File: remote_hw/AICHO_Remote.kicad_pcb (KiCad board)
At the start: 2 copper layers, 14 parts, among them J3 RJ45, U1 TPS54302

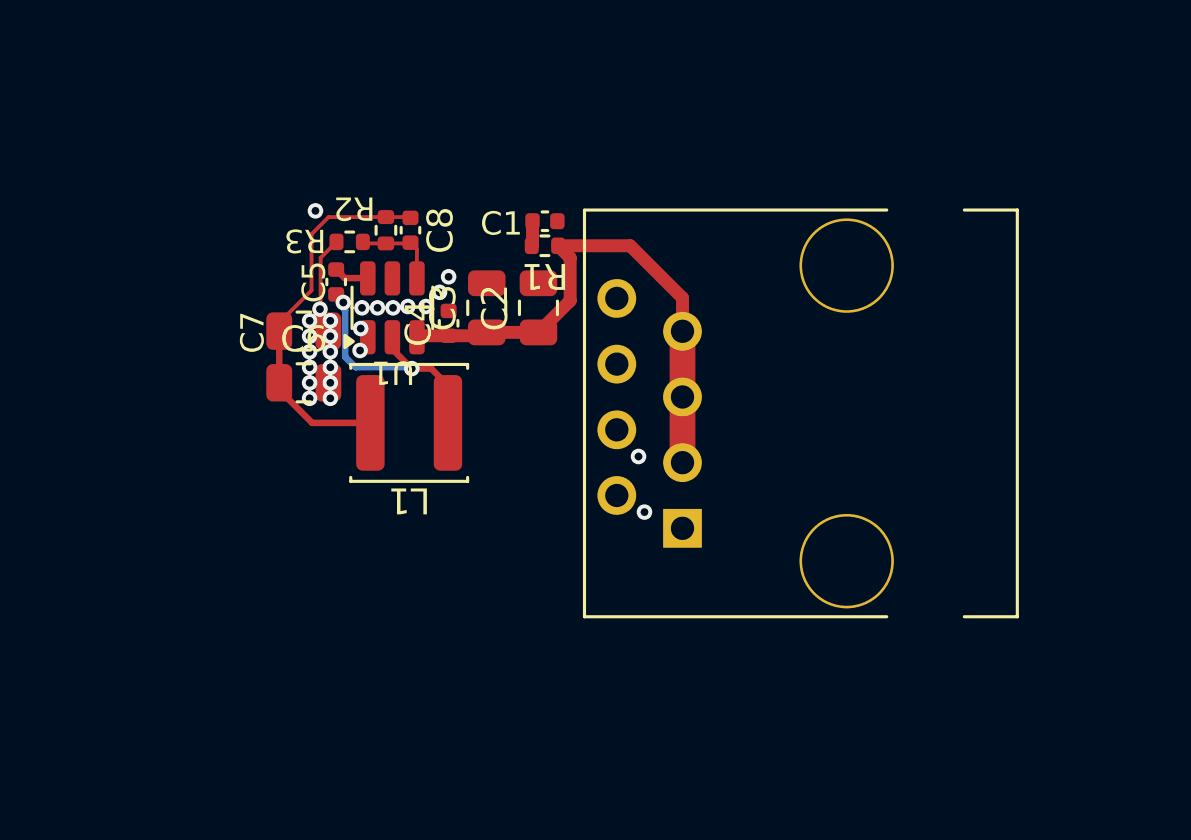
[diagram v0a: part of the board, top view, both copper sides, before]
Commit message: remote_hw: Finish layout & routing
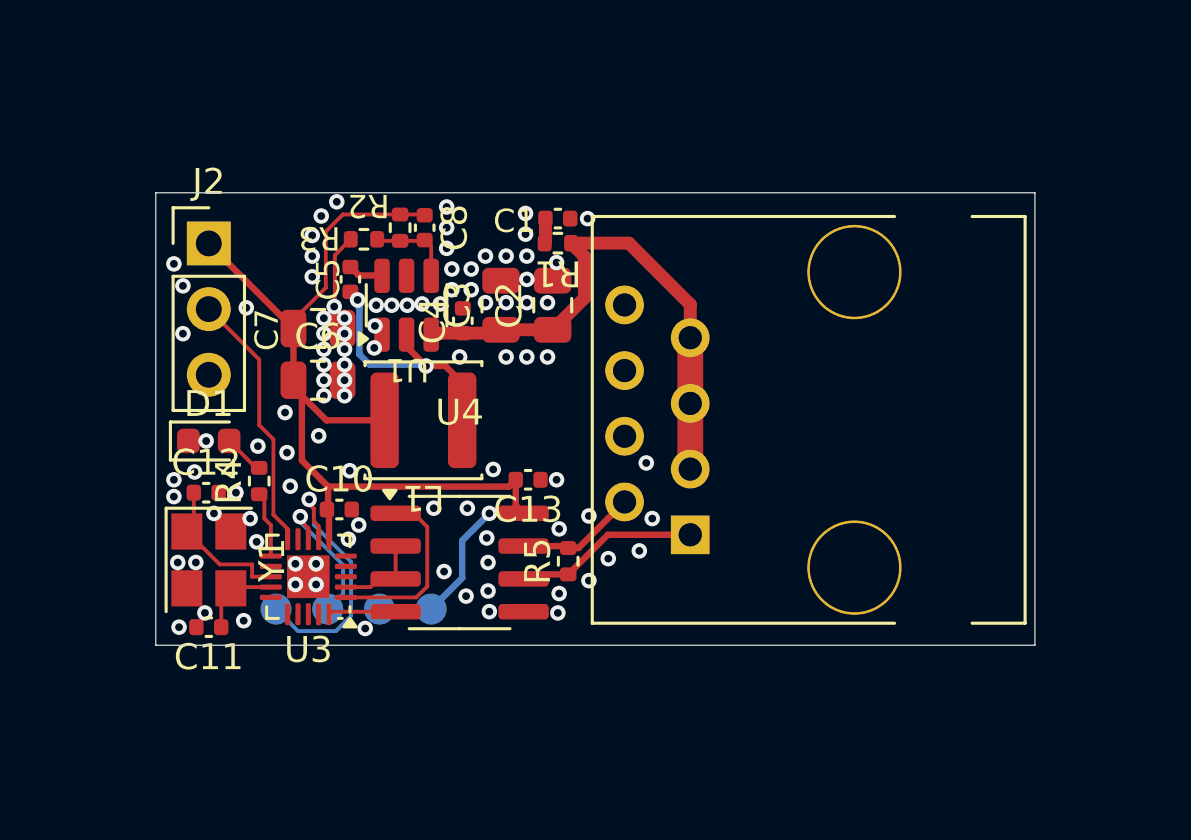
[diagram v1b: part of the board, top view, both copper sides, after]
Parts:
- added C10: 100n, Capacitor_SMD:C_0402_1005Metric, F.Cu at (69.1, 51.5)
- added C11: 15p, Capacitor_SMD:C_0402_1005Metric, F.Cu at (64.0, 56.0)
- added C12: 15p, Capacitor_SMD:C_0402_1005Metric, F.Cu at (64.0, 50.9)
- added C13: 100n, Capacitor_SMD:C_0402_1005Metric, F.Cu at (76.4, 50.4)
- added D1: White, LED_SMD:LED_0603_1608Metric, F.Cu at (64.0, 48.9)
- added J1: Conn_01x04, TestPoints_P2.00:TestPoints_1x04_P2.00, B.Cu at (69.7, 55.4)
- added J2: Conn_01x03_Pin, Connector_PinHeader_2.54mm:PinHeader_1x03_P2.54mm_Vertical, F.Cu at (64.0, 41.2)
- added R4: 6.8k, Resistor_SMD:R_0402_1005Metric, F.Cu at (66.0, 50.4)
- added R5: 100, Resistor_SMD:R_0402_1005Metric, F.Cu at (78.0, 53.5)
- added U3: PY32F003F18U6, Package_DFN_QFN:QFN-20-1EP_3x3mm_P0.4mm_EP1.65x1.65mm, F.Cu at (67.9, 54.1)
- added U4: SP485E, Package_SO:SOIC-8_3.9x4.9mm_P1.27mm, F.Cu at (73.8, 53.5)
- added Y1: 16MHz 9pF, Crystal:Crystal_SMD_3225-4Pin_3.2x2.5mm, F.Cu at (64.0, 53.5)
- moved C5 0.56 mm to (69.5, 42.6)
- moved C6 0.56 mm to (68.3, 46.5)
- moved C7 0.56 mm to (68.3, 44.5)
- moved C8 0.56 mm to (72.4, 40.6)
- moved C2 0.56 mm to (77.3, 43.6)
- moved C3 0.56 mm to (75.3, 43.6)
- moved L1 0.56 mm to (72.3, 48.0)
- moved R2 0.56 mm to (71.5, 40.6)
- moved R3 0.56 mm to (70.0, 41.0)
- moved U1 0.56 mm to (71.7, 43.6)
- moved C4 0.56 mm to (73.9, 44.2)
- moved C1 0.51 mm to (77.5, 40.2)
- moved R1 0.51 mm to (77.5, 41.2)
- moved J3 0.39 mm to (82.7, 52.5)
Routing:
- net +5V: track 14.7 -> 40.9 mm, vias 0 -> 1
- net /SWDIO: track 0.00 -> 10.4 mm, vias 0 -> 1
- net /LIGHT_SIG: track 0.00 -> 10.2 mm
- net /RS485_A: track 0.00 -> 7.15 mm
- net /UART_RX: track 0.00 -> 7.07 mm
- net Net-(U3-PF0): track 0.00 -> 5.87 mm
- net /SWCLK: track 0.00 -> 5.51 mm, vias 0 -> 1
- net /RS485_B: track 0.00 -> 4.67 mm
- net /DE: track 0.00 -> 3.33 mm
- net Net-(U3-PF1): track 0.00 -> 3.31 mm
- net /UART_TX: track 0.00 -> 2.61 mm
- net /ACT_LED: track 0.00 -> 2.58 mm
- net Net-(D1-A): track 0.00 -> 1.59 mm
- net GND: vias 25 -> 97
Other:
- board outline added: 34 x 17.5 mm

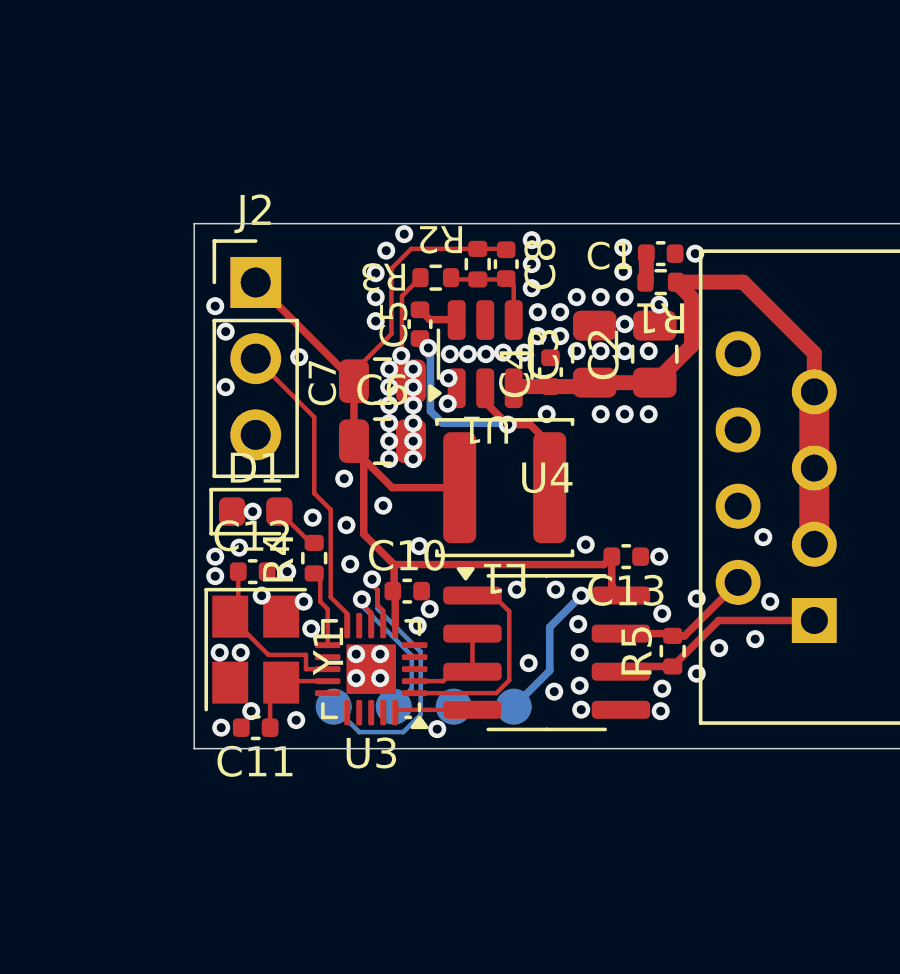
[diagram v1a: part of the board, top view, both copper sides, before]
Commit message: remote_hw: Adjust silkscreen
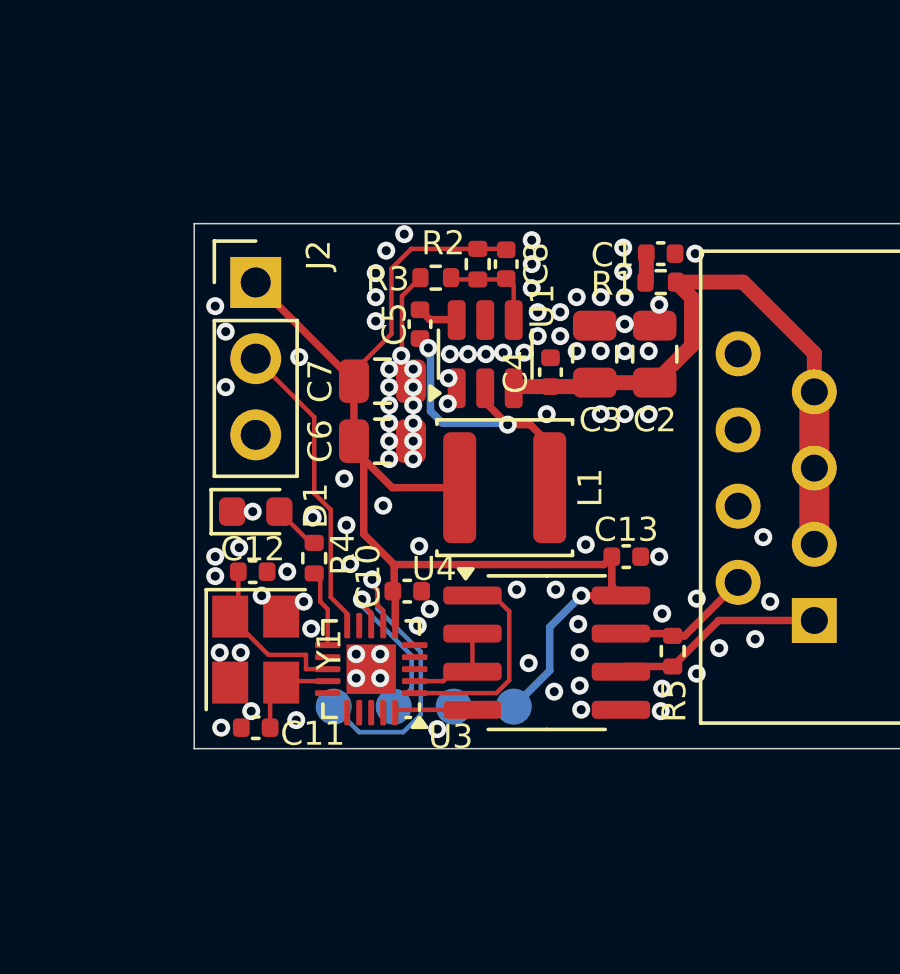
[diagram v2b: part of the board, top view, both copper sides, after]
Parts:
- added G***: LOGO, LOGO, B.Cu at (93.3, 44.4)
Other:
- board text added: "<25-"
- board text added: ">"
- board text added: "Rev. 1"
- board text added: "白露"

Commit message: remote_hw: Revise details
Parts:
- moved G*** 0.25 mm to (93.3, 44.6)
- renumbered U3 to U2, U4 to U3
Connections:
- U2 pad 12: unconnected-(U3-PF4-Pad12) -> (no net)
- U2 pad 15: unconnected-(U3-PF2-Pad15) -> (no net)
- U2 pad 16: unconnected-(U3-PA0-Pad16) -> (no net)
- U2 pad 17: unconnected-(U3-PA1-Pad17) -> (no net)
- U2 pad 18: unconnected-(U3-PA2-Pad18) -> (no net)
- U2 pad 19: unconnected-(U3-PA3-Pad19) -> (no net)
- U2 pad 3: unconnected-(U3-PA7-Pad3) -> (no net)
- U2 pad 5: unconnected-(U3-PA12-Pad5) -> (no net)
- U2 pad 9: unconnected-(U3-PB5-Pad9) -> (no net)
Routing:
- net GND: vias 97 -> 101

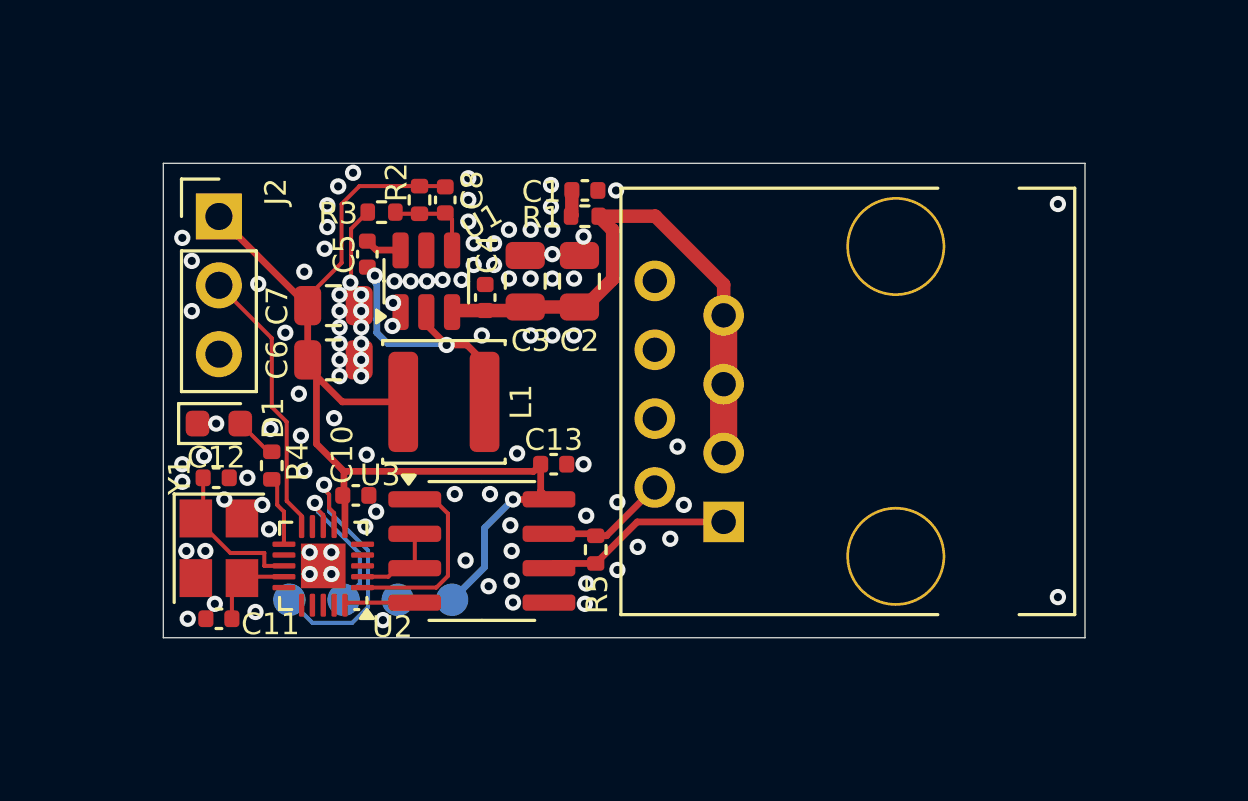
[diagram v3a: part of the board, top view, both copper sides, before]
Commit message: remote_hw: Further revise details
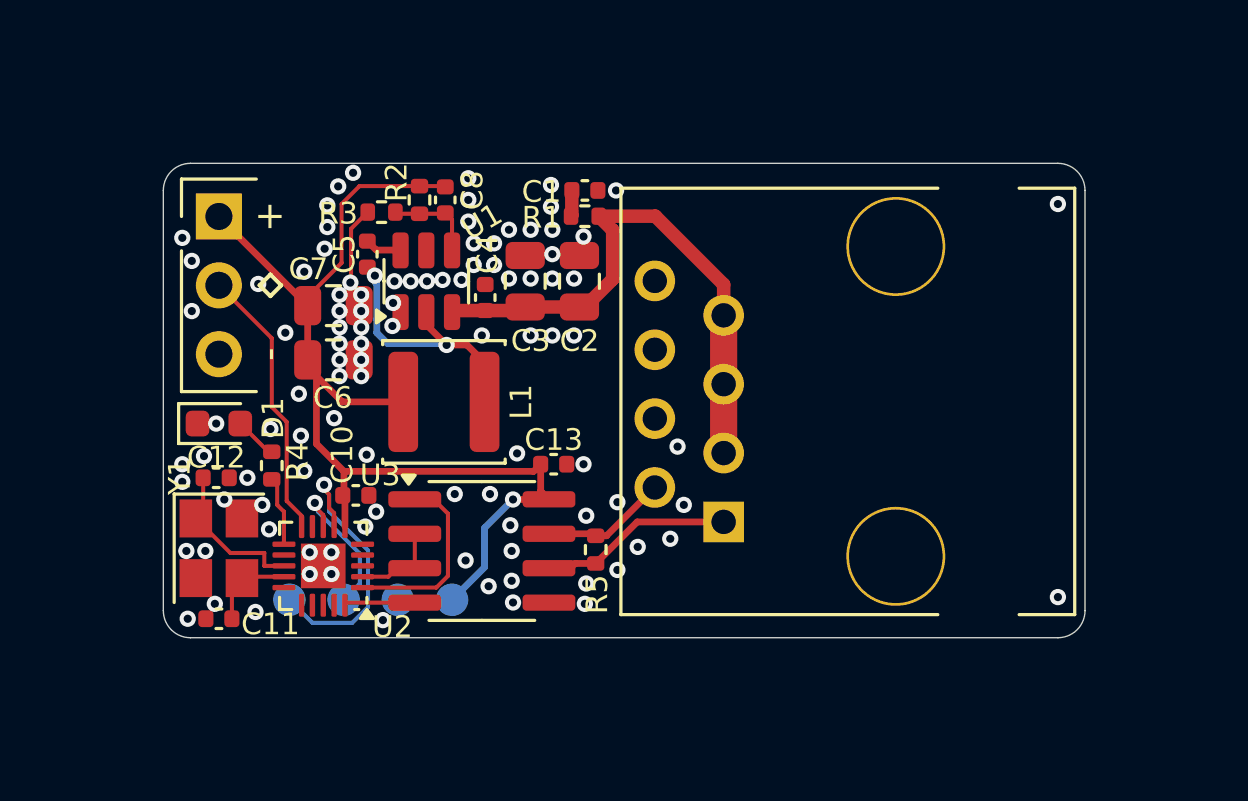
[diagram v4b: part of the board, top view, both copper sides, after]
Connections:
- U2 pad 12: (no net) -> unconnected-(U2-PF4-Pad12)
- U2 pad 15: (no net) -> unconnected-(U2-PF2-Pad15)
- U2 pad 16: (no net) -> unconnected-(U2-PA0-Pad16)
- U2 pad 17: (no net) -> unconnected-(U2-PA1-Pad17)
- U2 pad 18: (no net) -> unconnected-(U2-PA2-Pad18)
- U2 pad 19: (no net) -> unconnected-(U2-PA3-Pad19)
- U2 pad 3: (no net) -> unconnected-(U2-PA7-Pad3)
- U2 pad 5: (no net) -> unconnected-(U2-PA12-Pad5)
- U2 pad 9: (no net) -> unconnected-(U2-PB5-Pad9)
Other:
- outline, holes or cut-outs redrawn
- board text added: "+"
- board text added: "-"
- board text added: "ayu.land/aicho?id=R3_xx"

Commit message: remote_hw: Update component values with fabrication settings
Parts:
- R4: value 6.8k -> 4.7k
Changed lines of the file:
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@@
-			)
-		)
-		(property "LCSC PN" "C338080"
-			(at 0 0 90)
-			(unlocked yes)
-			(layer "F.Fab")
-			(hide yes)
-			(effects
-				(font
-					(size 1 1)
-					(thickness 0.15)
-				)
-			)
-		)
-		(property "Mfr PN" "C2012X5R1V226MT000E"
-			(at 0 0 90)
-			(unlocked yes)
-			(layer "F.Fab")
-			(hide yes)
-			(effects
-				(font
-					(size 1 1)
-					(thickness 0.15)
-				)
 			)
 		)
@@
 			)
 		)
-		(property "Value" "6.8k"
+		(property "Value" "4.7k"
 			(at 0 1.17 90)
 			(unlocked yes)
@@
 					(thickness 0.15)
 				)
-			)
-		)
-		(property "LCSC PN" "C338080"
-			(at 0 0 90)
-			(unlocked yes)
-			(layer "F.Fab")
-			(hide yes)
-			(effects
-				(font
-					(size 1 1)
-					(thickness 0.15)
-				)
-			)
-		)
-		(property "Mfr PN" "C2012X5R1V226MT000E"
-			(at 0 0 90)
-			(unlocked yes)
-			(layer "F.Fab")
-			(hide yes)
-			(effects
-				(font
-					(size 1 1)
-					(thickness 0.15)
-				)
